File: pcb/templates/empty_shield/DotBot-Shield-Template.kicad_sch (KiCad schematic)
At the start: 23 parts, among them J1 Conn_01x04, J1 Conn_01x10, Q1 NX6008NBKWX, Q2 NX6008NBKWX, Q3 NX6008NBKWX, U3 ISM330DHCXTR, U4 LIS3MDL, U4 TS4231

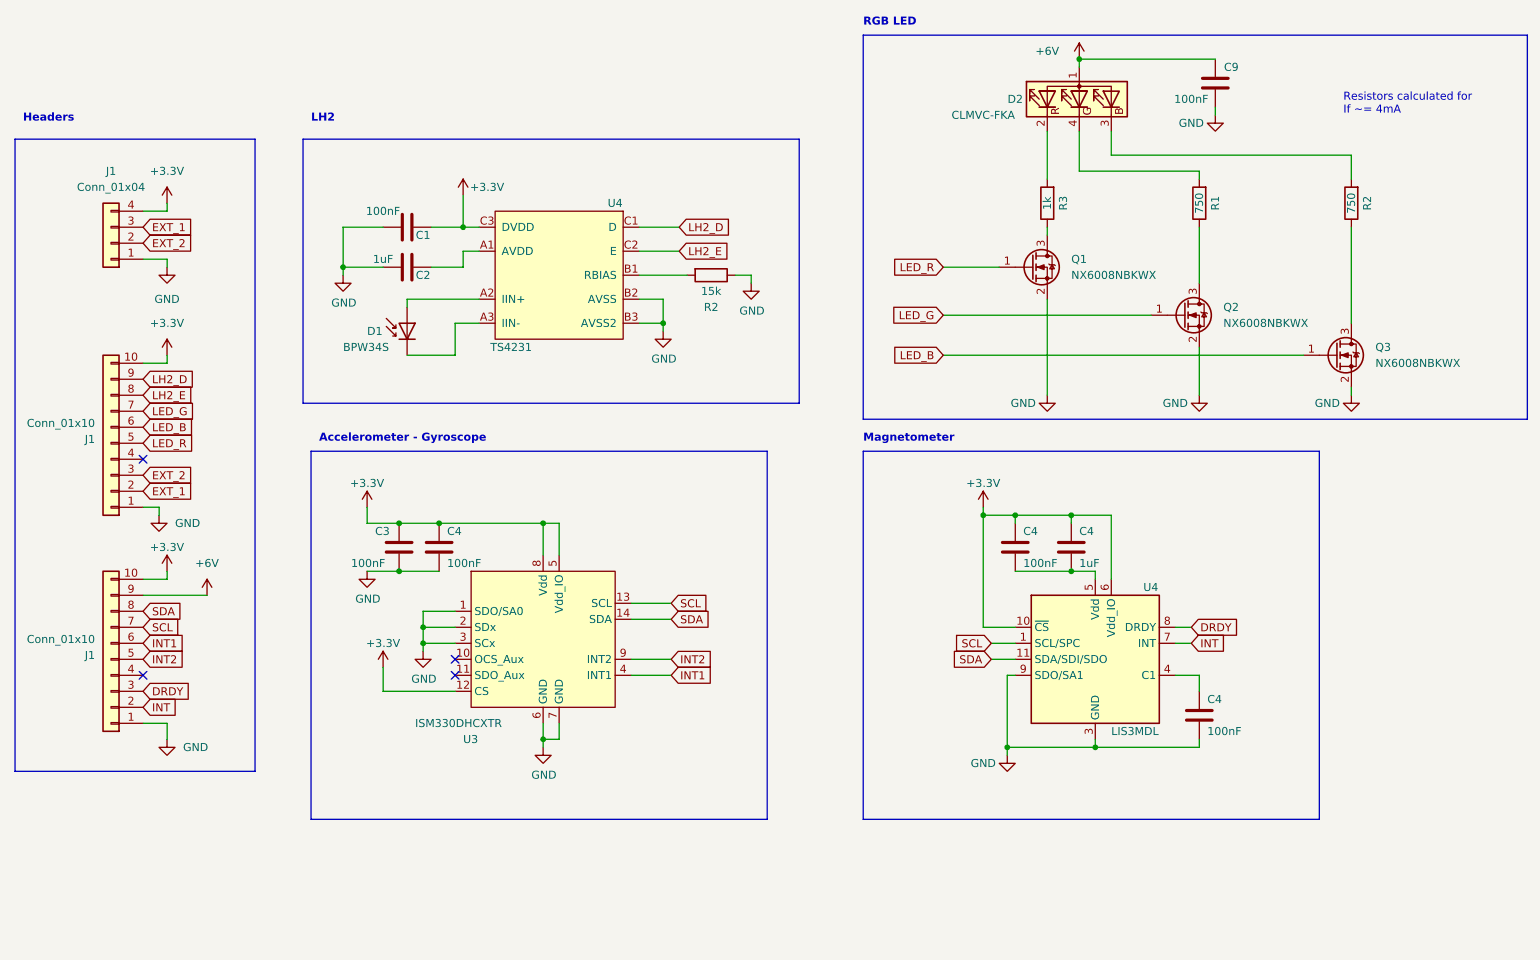
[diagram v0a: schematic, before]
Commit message: #12 remove unneeded components from the schematics
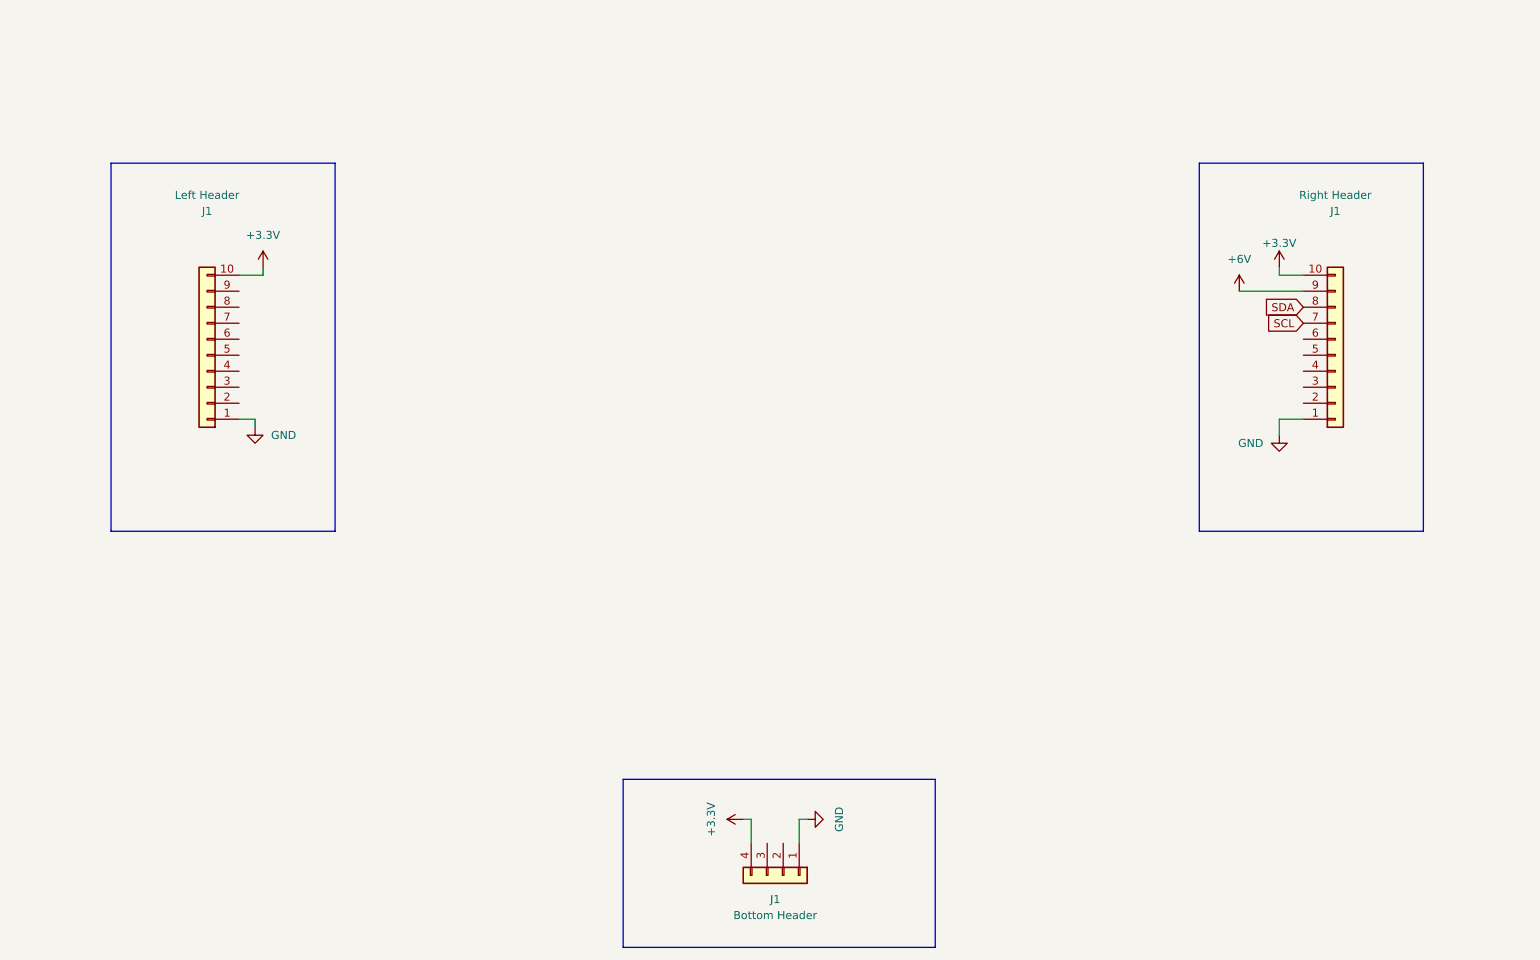
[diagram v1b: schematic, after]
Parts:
- removed C1, C3, C4 (x3), C9: 100nF, Capacitor_SMD:C_0603_1608Metric, symbol Device:C
- removed C2, C4: 1uF, Capacitor_SMD:C_0603_1608Metric, symbol Device:C
- removed D1: BPW34S, DotBot:BPW34, symbol Device:D_Photo
- removed D2: CLMVC-FKA, LED_SMD:LED_Cree-PLCC4_2x2mm_CW, symbol Device:LED_ARBG
- removed Q1, Q2, Q3: NX6008NBKWX, Package_TO_SOT_SMD:SOT-323_SC-70, symbol Device:Q_NMOS_GSD
- removed R1, R2: 750, Resistor_SMD:R_0603_1608Metric, symbol Device:R
- removed R2: 15k, Resistor_SMD:R_0603_1608Metric, symbol Device:R
- removed R3: 1k, Resistor_SMD:R_0603_1608Metric, symbol Device:R
- removed U3: ISM330DHCXTR, Package_LGA:Bosch_LGA-14_3x2.5mm_P0.5mm, symbol DotBot:ISM330DHCXTR
- removed U4: TS4231, DotBot:TS4231, symbol DotBot:TS4231
- removed U4: LIS3MDL, Package_LGA:LGA-12_2x2mm_P0.5mm, symbol Sensor_Magnetic:LIS3MDL
- J1: value Conn_01x10 -> Right Header
- J1: value Conn_01x04 -> Bottom Header
- J1: value Conn_01x10 -> Left Header
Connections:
- net DRDY: no longer names the net of J1.3 (Pin_3)
- net EXT_1: no longer names the net of J1.3 (Pin_3)
- net EXT_1: no longer J1.2 (Pin_2)
- net EXT_2: no longer names the net of J1.2 (Pin_2)
- net EXT_2: no longer J1.3 (Pin_3)
- net INT: no longer names the net of J1.2 (Pin_2)
- net INT1: no longer names the net of J1.6 (Pin_6)
- net INT2: no longer names the net of J1.5 (Pin_5)
- net LED_B: no longer names the net of J1.6 (Pin_6)
- net LED_G: no longer names the net of J1.7 (Pin_7)
- net LED_R: no longer names the net of J1.5 (Pin_5)
- net LH2_D: no longer names the net of J1.9 (Pin_9)
- net LH2_E: no longer names the net of J1.8 (Pin_8)
- no-connect marks 4 -> 0
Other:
- note removed: "Accelerometer - Gyroscope"
- note removed: "Headers"
- note removed: "LH2"
- note removed: "Magnetometer"
- note removed: "RGB LED"
- note removed: "Resistors calculated for If ~= 4mA"
- title: DotBot lighthouse shield -> DotBot Template Shield
- moved on the sheet: J1
